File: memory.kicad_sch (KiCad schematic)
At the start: 32 parts, among them U2 IS43TR16640C-125JBL

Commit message: More DDR Routing
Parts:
- R27: footprint Resistor_SMD:R_0402_1005Metric -> Resistor_SMD:R_0201_0603Metric
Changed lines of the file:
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@@
 			)
 		)
-		(property "Footprint" "Resistor_SMD:R_0402_1005Metric"
+		(property "Footprint" "Resistor_SMD:R_0201_0603Metric"
 			(at 150.368 185.42 0)
 			(effects

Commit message: Updated memory added 33ohm resistors
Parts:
- added R41, R45, R47: 33, Resistor_SMD:R_0201_0603Metric, symbol SparkFun-Resistor:R
- added R53, R54, R55, R56, R57, R58, R59, R60, R61, R62, R63, R64, R65, R66, R67, R68, R69, R70, R71, R72, R73, R74, R75: 33, Resistor_SMD:R_0402_1005Metric, symbol SparkFun-Resistor:R
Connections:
- net A0: now also R60.2; no longer U2.N3 (A0)
- net A1: now also R61.2; no longer U2.P7 (A1)
- net A10: now also R58.2; no longer U2.L7 (A10/AP)
- net A11: now also R57.2; no longer U2.R7 (A11)
- net A12: now also R56.2; no longer U2.N7 (A12/BC#)
- net A13: now also R55.2; no longer U2.T3 (A13)
- net A14: now also R54.2; no longer U2.T7 (A14)
- net A15: now also R53.2; no longer U2.M7 (A15)
- net A2: now also R62.2; no longer U2.P3 (A2)
- net A3: now also R63.2; no longer U2.N2 (A3)
- net A4: now also R64.2; no longer U2.P8 (A4)
- net A5: now also R65.2; no longer U2.P2 (A5)
- net A6: now also R66.2; no longer U2.R8 (A6)
- net A7: now also R68.2; no longer U2.R2 (A7)
- net A8: now also R67.2; no longer U2.T8 (A8)
- net A9: now also R59.2; no longer U2.R3 (A9)
- net CAS: now also R74.1; no longer U2.K3 (CAS#)
- net CKE: now also R71.1; no longer U2.K9 (CKE)
- net CS: now also R72.1; no longer U2.L2 (CS#)
- net DDR_BA0: now also R41.2; no longer U2.M2 (BA0)
- net DDR_BA1: now also R45.2; no longer U2.N8 (BA1)
- net DDR_BA2: now also R47.2; no longer U2.M3 (BA2)
- net ODT: now also R69.1; no longer U2.K1 (ODT)
- net RAS: now also R75.1; no longer U2.J3 (RAS#)
- net RESET: now also R70.1; no longer U2.T2 (RESET#)
- net WE: now also R73.1; no longer U2.L3 (WE#)
- new net: R53.1, U2.M7 (A15)
- new net: R62.1, U2.P3 (A2)
- new net: R41.1, U2.M2 (BA0)
- new net: R60.1, U2.N3 (A0)
- new net: R58.1, U2.L7 (A10/AP)
- new net: R56.1, U2.N7 (A12/BC#)
- new net: R59.1, U2.R3 (A9)
- new net: R74.2, U2.K3 (CAS#)
- new net: R54.1, U2.T7 (A14)
- new net: R64.1, U2.P8 (A4)
- new net: R65.1, U2.P2 (A5)
- new net: R55.1, U2.T3 (A13)
- new net: R68.1, U2.R2 (A7)
- new net: R69.2, U2.K1 (ODT)
- new net: R67.1, U2.T8 (A8)
- new net: R45.1, U2.N8 (BA1)
- new net: R73.2, U2.L3 (WE#)
- new net: R75.2, U2.J3 (RAS#)
- new net: R71.2, U2.K9 (CKE)
- new net: R72.2, U2.L2 (CS#)
- new net: R47.1, U2.M3 (BA2)
- new net: R63.1, U2.N2 (A3)
- new net: R61.1, U2.P7 (A1)
- new net: R57.1, U2.R7 (A11)
- new net: R66.1, U2.R8 (A6)
- new net: R70.2, U2.T2 (RESET#)
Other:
- moved on the sheet: C1, C2, C3, C4, C5, C6, C7, R17, R18, R19, R20, R21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

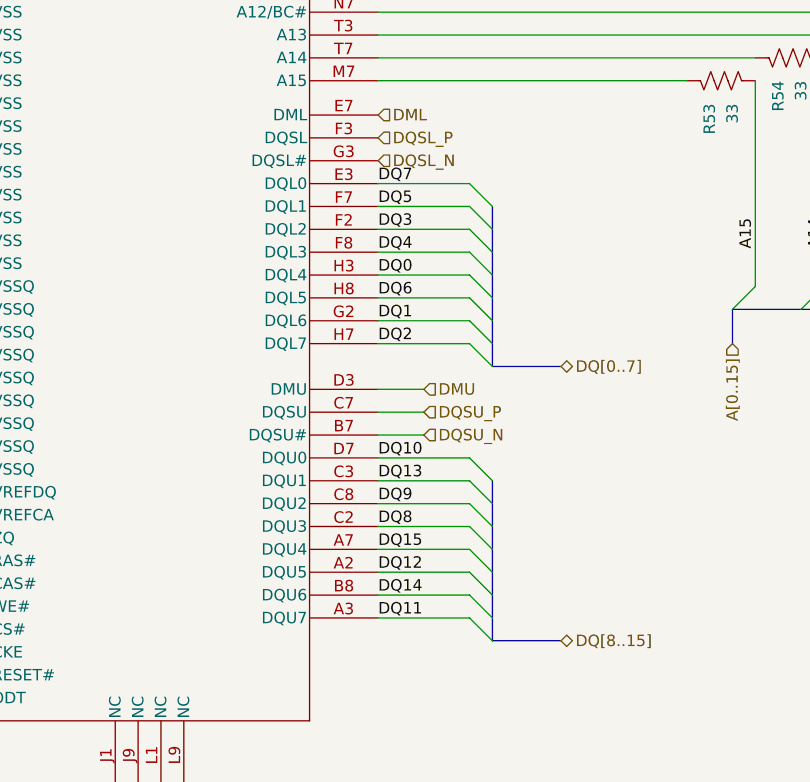
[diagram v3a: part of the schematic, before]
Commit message: DDR Routing commenced
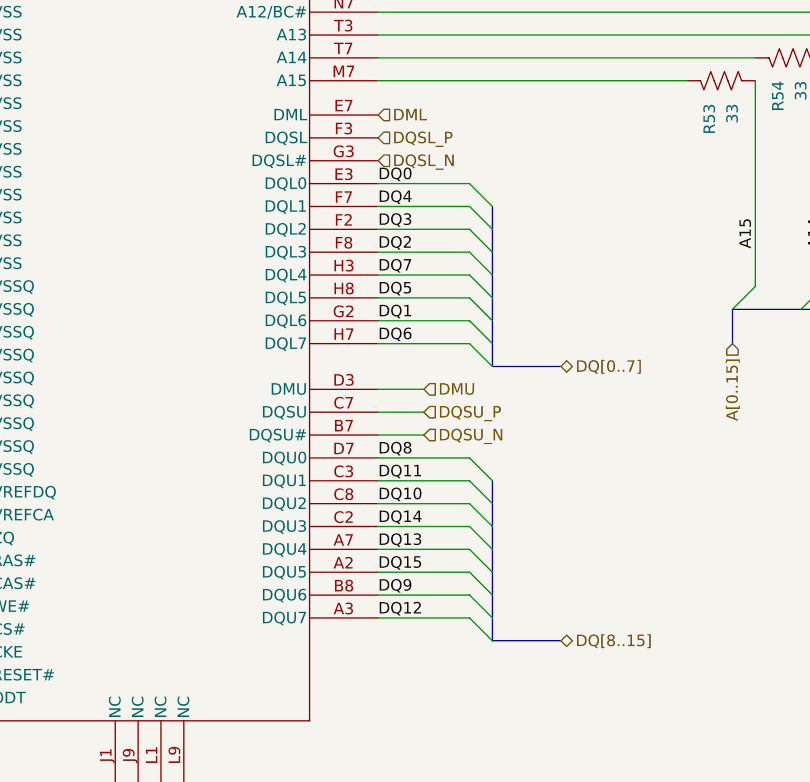
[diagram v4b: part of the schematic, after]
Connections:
- net DQ0: now also U2.E3 (DQL0); no longer U2.H3 (DQL4)
- net DQ10: now also U2.C8 (DQU2); no longer U2.D7 (DQU0)
- net DQ11: now also U2.C3 (DQU1); no longer U2.A3 (DQU7)
- net DQ12: now also U2.A3 (DQU7); no longer U2.A2 (DQU5)
- net DQ13: now also U2.A7 (DQU4); no longer U2.C3 (DQU1)
- net DQ14: now also U2.C2 (DQU3); no longer U2.B8 (DQU6)
- net DQ15: now also U2.A2 (DQU5); no longer U2.A7 (DQU4)
- net DQ2: now also U2.F8 (DQL3); no longer U2.H7 (DQL7)
- net DQ4: now also U2.F7 (DQL1); no longer U2.F8 (DQL3)
- net DQ5: now also U2.H8 (DQL5); no longer U2.F7 (DQL1)
- net DQ6: now also U2.H7 (DQL7); no longer U2.H8 (DQL5)
- net DQ7: now also U2.H3 (DQL4); no longer U2.E3 (DQL0)
- net DQ8: now also U2.D7 (DQU0); no longer U2.C2 (DQU3)
- net DQ9: now also U2.B8 (DQU6); no longer U2.C8 (DQU2)
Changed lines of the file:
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@@
 		)
 	)
-	(label "DQ15"
+	(label "DQ13"
 		(at 149.86 135.89 0)
 		(effects
@@
 		)
 	)
-	(label "DQ14"
+	(label "DQ9"
 		(at 149.86 140.97 0)
 		(effects
@@
 		)
 	)
-	(label "DQ4"
+	(label "DQ2"
 		(at 149.86 102.87 0)
 		(effects
@@
 		)
 	)
-	(label "DQ6"
+	(label "DQ5"
 		(at 149.86 107.95 0)
 		(effects
@@
 		)
 	)
-	(label "DQ2"
+	(label "DQ6"
 		(at 149.86 113.03 0)
 		(effects
@@
 		)
 	)
-	(label "DQ11"
+	(label "DQ12"
 		(at 149.86 143.51 0)
 		(effects
@@
 		)
 	)
-	(label "DQ7"
+	(label "DQ0"
 		(at 149.86 95.25 0)
 		(effects
@@
 		)
 	)
-	(label "DQ10"
+	(label "DQ8"
 		(at 149.86 125.73 0)
 		(effects
@@
 		)
 	)
-	(label "DQ8"
+	(label "DQ14"
 		(at 149.86 133.35 0)
 		(effects
@@
 		)
 	)
-	(label "DQ5"
+	(label "DQ4"
 		(at 149.86 97.79 0)
 		(effects
@@
 		)
 	)
-	(label "DQ9"
+	(label "DQ10"
 		(at 149.86 130.81 0)
 		(effects
@@
 		)
 	)
-	(label "DQ0"
+	(label "DQ7"
 		(at 149.86 105.41 0)
 		(effects
@@
 		)
 	)
-	(label "DQ13"
+	(label "DQ11"
 		(at 149.86 128.27 0)
 		(effects
@@
 		)
 	)
-	(label "DQ12"
+	(label "DQ15"
 		(at 149.86 138.43 0)
 		(effects

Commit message: DDR routing
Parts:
- R41, R45, R47: footprint Resistor_SMD:R_0201_0603Metric -> Resistor_SMD:R_0402_1005Metric
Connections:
- net DQ4: now also U2.H7 (DQL7); no longer U2.F7 (DQL1)
- net DQ6: now also U2.F7 (DQL1); no longer U2.H7 (DQL7)
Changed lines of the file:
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@@
 		)
 	)
-	(label "DQ6"
+	(label "DQ4"
 		(at 149.86 113.03 0)
 		(effects
@@
 		)
 	)
-	(label "DQ4"
+	(label "DQ6"
 		(at 149.86 97.79 0)
 		(effects
@@
 			)
 		)
-		(property "Footprint" "Resistor_SMD:R_0201_0603Metric"
+		(property "Footprint" "Resistor_SMD:R_0402_1005Metric"
 			(at 171.45 22.352 0)
 			(effects
@@
 			)
 		)
-		(property "Footprint" "Resistor_SMD:R_0201_0603Metric"
+		(property "Footprint" "Resistor_SMD:R_0402_1005Metric"
 			(at 171.45 31.242 0)
 			(effects
@@
 			)
 		)
-		(property "Footprint" "Resistor_SMD:R_0201_0603Metric"
+		(property "Footprint" "Resistor_SMD:R_0402_1005Metric"
 			(at 171.45 40.132 0)
 			(effects

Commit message: DDR complete needs polish
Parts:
- removed R70: 33, Resistor_SMD:R_0402_1005Metric, symbol SparkFun-Resistor:R
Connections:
- net RESET: now also U2.T2 (RESET#)
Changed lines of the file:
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@@
 	(wire
 		(pts
-			(xy 27.94 149.86) (xy 29.21 149.86)
+			(xy 27.94 149.86) (xy 99.06 149.86)
 		)
 		(stroke
@@
 	(wire
 		(pts
-			(xy 36.83 149.86) (xy 99.06 149.86)
-		)
-		(stroke
-			(width 0)
-			(type default)
-		)
-	)
-	(wire
-		(pts
 			(xy 149.86 73.66) (xy 214.63 73.66)
 		)
@@
 					(unit 1)
 				)
-			)
-		)
-	)
-	(symbol
-		(lib_id "SparkFun-Resistor:R")
-		(at 33.02 149.86 180)
-		(unit 1)
-		(exclude_from_sim no)
-		(in_bom yes)
-		(on_board yes)
-		(dnp no)
-		(property "Reference" "R70"
-			(at 31.7499 147.32 90)
-			(effects
-				(font
-					(size 1.27 1.27)
-				)
-				(justify right)
-			)
-		)
-		(property "Value" "33"
-			(at 34.2899 147.32 90)
-			(effects
-				(font
-					(size 1.27 1.27)
-				)
-				(justify right)
-			)
-		)
-		(property "Footprint" "Resistor_SMD:R_0402_1005Metric"
-			(at 33.02 145.288 0)
-			(effects
-				(font
-					(size 1.27 1.27)
-				)
-				(hide yes)
-			)
-		)
-		(property "Datasheet" ""
-			(at 34.29 140.97 0)
-			(effects
-				(font
-					(size 1.27 1.27)
-				)
-				(hide yes)
-			)
-		)
-		(property "Description" "Resistor"
-			(at 33.02 138.43 0)
-			(effects
-				(font
-					(size 1.27 1.27)
-				)
-				(hide yes)
-			)
-		)
-		(property "Precision" "1%"
-			(at 36.576 147.066 90)
-			(effects
-				(font
-					(size 1.27 1.27)
-				)
-				(justify right)
-				(hide yes)
-			)
-		)
-		(pin "2"
-		)
-		(pin "1"
-		)
-		(instances
-			(project "SBC"
-				(path "/21bb932a-ec67-4661-9215-0551f718d1c0/1a39d522-2eb7-49c0-a4cb-6db909b7fe44"
-					(reference "R70")
-					(unit 1)
-				)

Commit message: DDR
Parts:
- removed R69: 33, Resistor_SMD:R_0402_1005Metric, symbol SparkFun-Resistor:R
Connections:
- net ODT: now also U2.K1 (ODT)
- net A15_R: now reaches R53.1, U2.M7 (A15)
- net A2_R: now reaches R62.1, U2.P3 (A2)
- net DDR_BA0_R: now reaches R41.1, U2.M2 (BA0)
- net A0_R: now reaches R60.1, U2.N3 (A0)
- net A10_R: now reaches R58.1, U2.L7 (A10/AP)
- net A12_R: now reaches R56.1, U2.N7 (A12/BC#)
- net A9_R: now reaches R59.1, U2.R3 (A9)
- net CAS_R: now reaches R74.2, U2.K3 (CAS#)
- net A14_R: now reaches R54.1, U2.T7 (A14)
- net A4_R: now reaches R64.1, U2.P8 (A4)
- net A5_R: now reaches R65.1, U2.P2 (A5)
- net A13_R: now reaches R55.1, U2.T3 (A13)
- net A7_R: now reaches R68.1, U2.R2 (A7)
- net A8_R: now reaches R67.1, U2.T8 (A8)
- net DDR_BA1_R: now reaches R45.1, U2.N8 (BA1)
- net WE_R: now reaches R73.2, U2.L3 (WE#)
- net RAS_R: now reaches R75.2, U2.J3 (RAS#)
- net CKE_R: now reaches R71.2, U2.K9 (CKE)
- net CS_R: now reaches R72.2, U2.L2 (CS#)
- net DDR_BA2_R: now reaches R47.1, U2.M3 (BA2)
- net A3_R: now reaches R63.1, U2.N2 (A3)
- net A1_R: now reaches R61.1, U2.P7 (A1)
- net A11_R: now reaches R57.1, U2.R7 (A11)
- net A6_R: now reaches R66.1, U2.R8 (A6)

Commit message: DDR Routing more
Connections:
- net DDR_BA0_R renamed BA0_R
- net DDR_BA1_R renamed BA1_R
- net DDR_BA2_R renamed BA2_R
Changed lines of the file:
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@@
 		)
 	)
-	(label "DDR_BA1_R"
+	(label "BA1_R"
 		(at 151.13 33.02 0)
 		(effects
@@
 		)
 	)
-	(label "DDR_BA0_R"
+	(label "BA0_R"
 		(at 151.13 30.48 0)
 		(effects
@@
 		)
 	)
-	(label "DDR_BA2_R"
+	(label "BA2_R"
 		(at 151.13 35.56 0)
 		(effects
